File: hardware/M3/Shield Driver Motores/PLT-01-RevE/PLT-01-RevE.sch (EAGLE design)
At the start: 21 parts, among them IC1 L293D, IC2 L293D, X1 22-23-2021, X2 22-23-2021, X3 22-23-2021, X4 22-23-2021, X5 22-23-2021

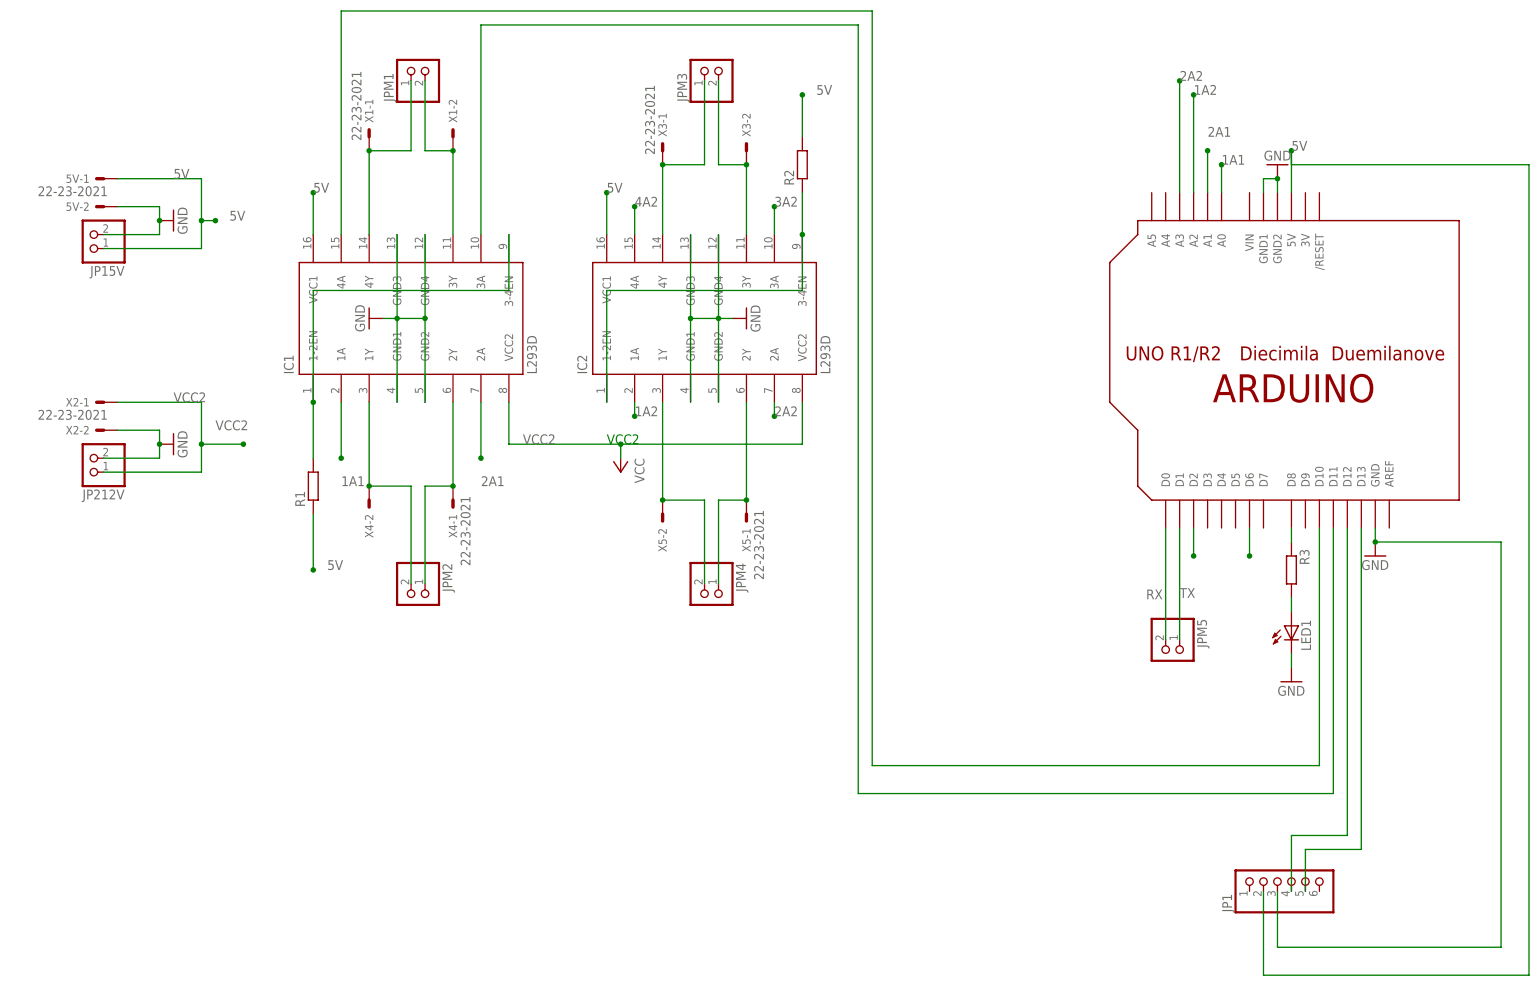
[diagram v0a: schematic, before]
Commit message: Se agrega bluettoth a placa M3 control de motores. RevE
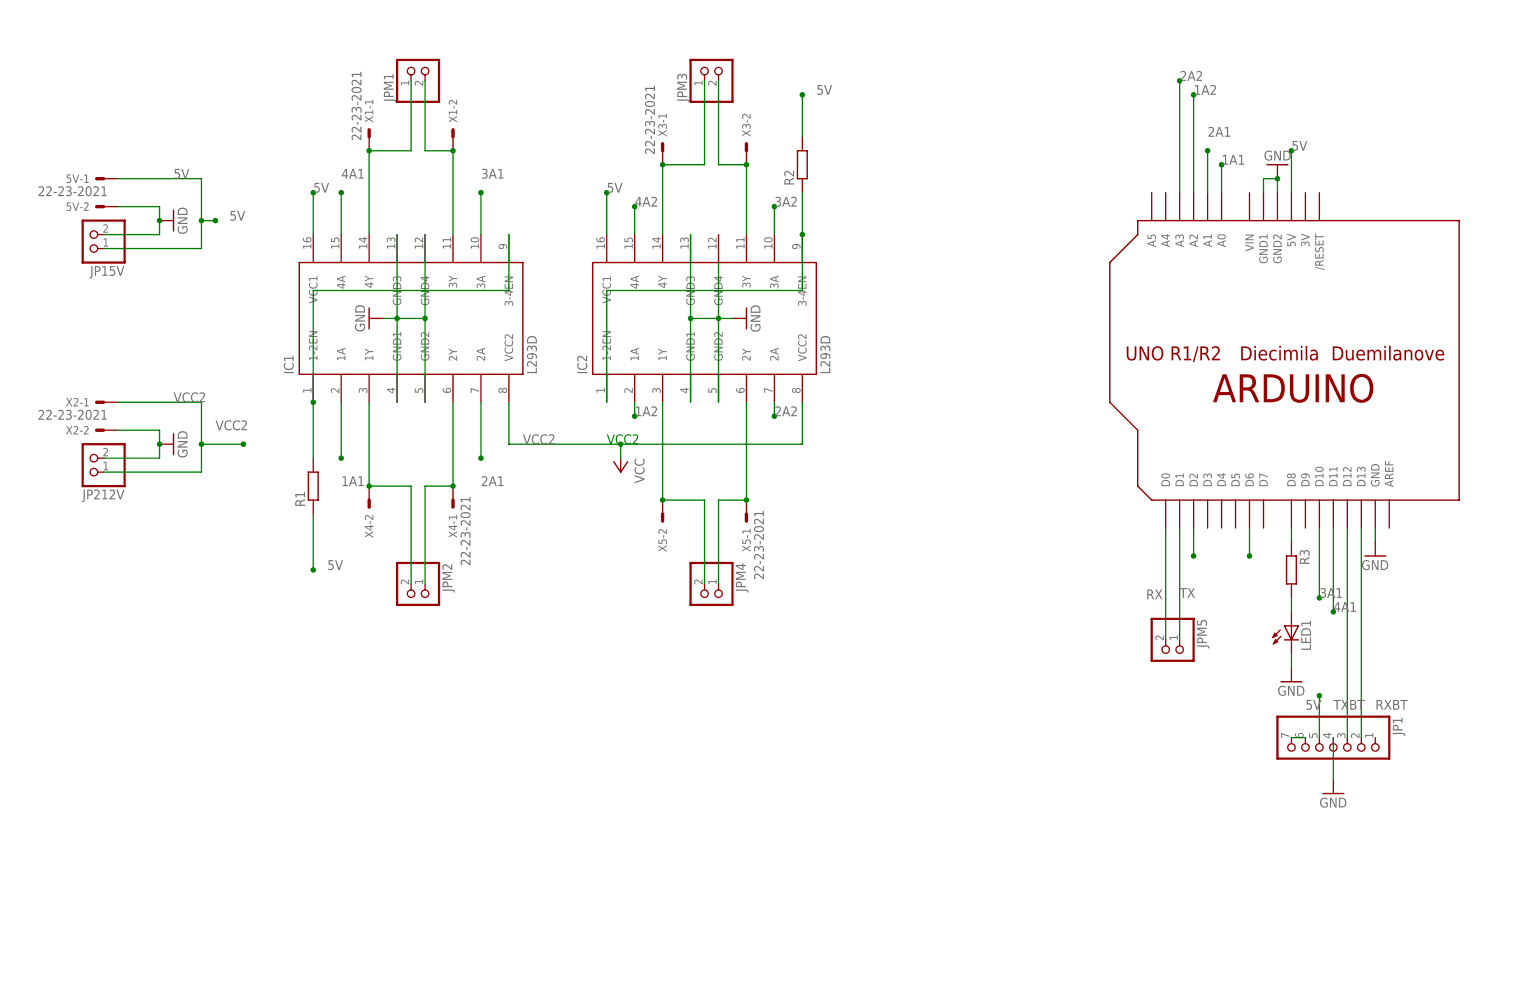
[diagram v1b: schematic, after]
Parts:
- JP1: device pinhead:PINHD-1X6 -> pinhead:PINHD-1X7
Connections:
- removed net N$11 (its old number): IC1.3A, U$1.D11
- removed net N$19: JP1.5, U$1.D13
- removed net N$22: IC1.4A, U$1.D10
- new net 3A1: IC1.3A, U$1.D10
- new net 4A1: IC1.4A, U$1.D11
- new net RXBT: JP1.2, U$1.D13
- new net TXBT: JP1.3, U$1.D12
- net 5V: now also JP1.5; no longer JP1.2
- net GND: now also JP1.4; no longer IC2.GND4, JP1.3
- net N$13: now also JP1.6, JP1.7; no longer JP1.4, U$1.D12
